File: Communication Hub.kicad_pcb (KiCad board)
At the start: 4 copper layers, 105 x 78.9 mm, 89 parts, among them J1 USB_B, J10 RS485, J11 RS422, J2 USB_A, J3 U5 TX RX, J4 U6 TX RX, J5 U7 TX RX, J6 RJ45, J7 RJ45, J8 RJ45, J9 CAN, U1 AMS1117-3.3, U10 MAX490E, U11 TPS2553DBVR, U12 TPS2553DBVR, U13 TPS2553DBVR, U2 USBLC6-2SC6, U3 USB2514B_Bi, U4 USBLC6-2SC6, U5 CP2102N-Axx-xQFN28, U6 CP2102N-Axx-xQFN28, U7 CP2102N-Axx-xQFN28, U8 TPS2553DBVR, U9 MAX3485, Y2 24Mhz

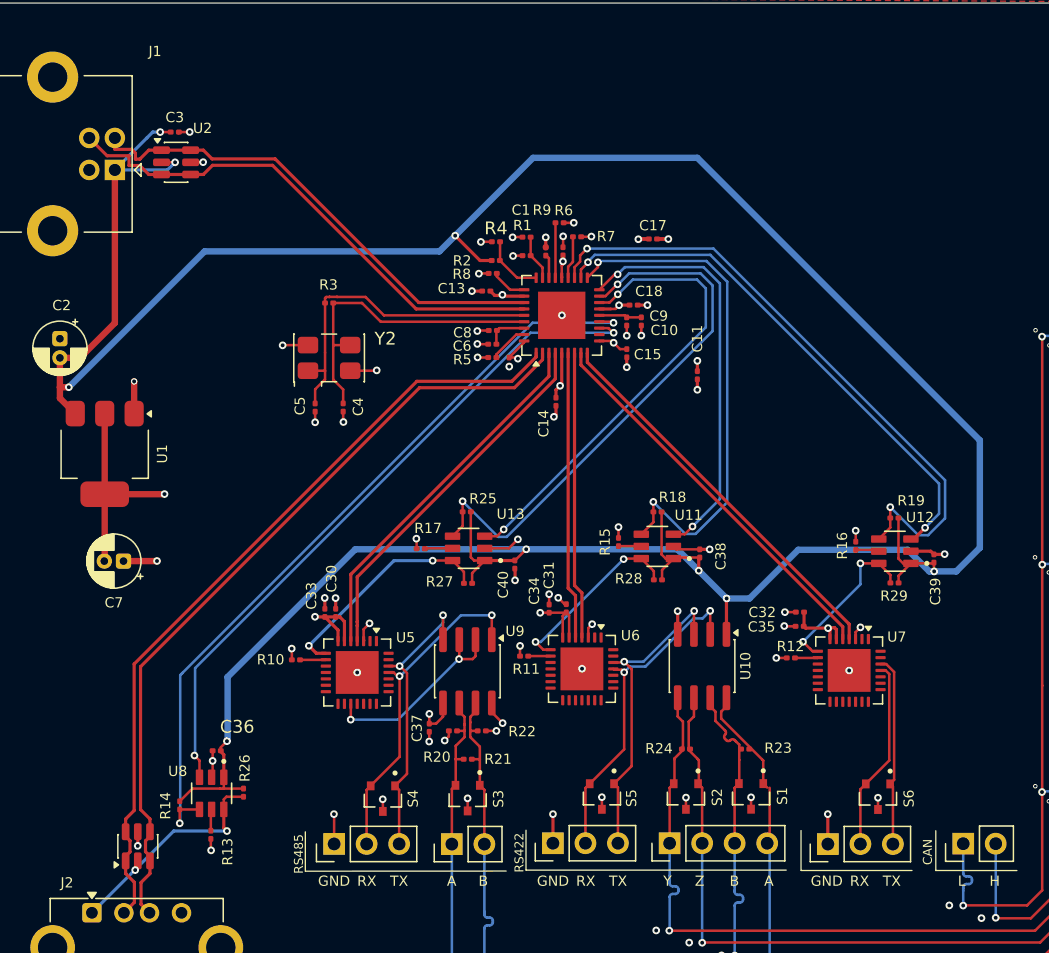
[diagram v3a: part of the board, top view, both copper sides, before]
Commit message: Corrections to PCB (modified passive components size) Corrections to schematics(addes some capacitors and other corrections)
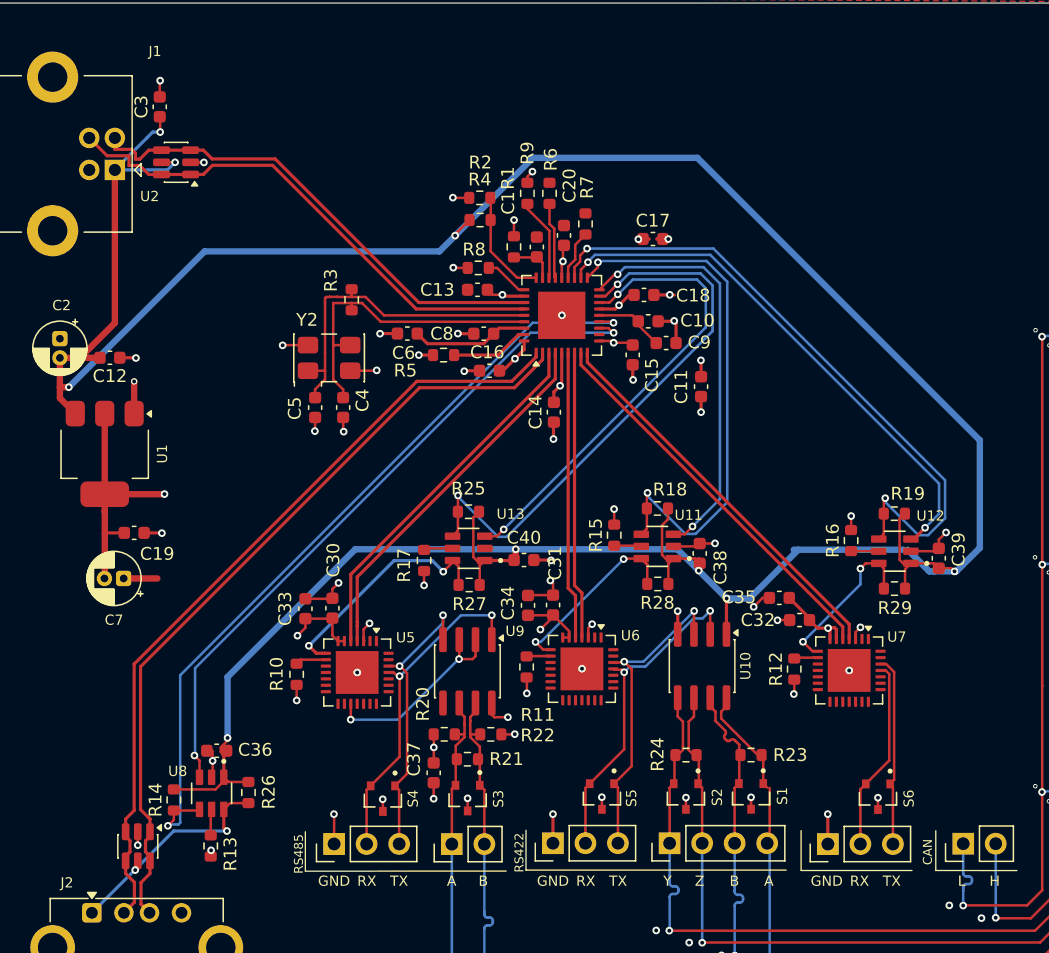
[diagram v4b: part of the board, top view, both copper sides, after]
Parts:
- added C12: 0.1uF, Capacitor_SMD:C_0603_1608Metric, F.Cu at (42.4, 88.0)
- added C19: 0.1uF, Capacitor_SMD:C_0603_1608Metric, F.Cu at (44.3, 101.6)
- C1, C10, C11, C13, C14, C15, C16, C17, C18, C20, C3, C30, C31, C32, C33, C34, C35, C36, C37, C38, C39, C4, C40, C5, C6, C8, C9: footprint Capacitor_SMD:C_0201_0603Metric -> Capacitor_SMD:C_0603_1608Metric
- R1, R10, R11, R12, R13, R14, R15, R16, R17, R18, R19, R2, R20, R21, R22, R23, R24, R25, R26, R27, R28, R29, R3, R4, R5, R6, R7, R8, R9: footprint Resistor_SMD:R_0201_0603Metric -> Resistor_SMD:R_0603_1608Metric
- moved C6 6.69 mm to (65.6, 86.1)
- moved R9 4.76 mm to (75.0, 75.1)
- moved R5 3.81 mm to (68.4, 87.7)
- moved R4 3.66 mm to (71.3, 75.5)
- moved C37 3.54 mm to (67.7, 120.4), turned to 90 degrees
- moved R2 3.39 mm to (71.3, 77.2)
- moved C35 2.73 mm to (94.7, 106.7)
- moved C9 2.57 mm to (85.8, 86.8), turned to 180 degrees
- moved R6 2.43 mm to (76.7, 75.1), turned to -90 degrees
- moved C3 2.30 mm to (46.3, 68.3), turned to 90 degrees
- moved R3 1.78 mm to (61.3, 83.4), turned to 90 degrees
- moved C16 1.68 mm to (72.0, 89.0), turned to 0 degrees
- moved C10 1.68 mm to (84.4, 85.1), turned to 180 degrees
- moved C34 1.67 mm to (75.0, 107.3)
- moved C33 1.55 mm to (57.6, 107.6)
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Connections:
- U2 pad 1: /DN -> /DP
- U2 pad 2: VBUS -> GND
- U2 pad 3: /DP -> /DN
- U2 pad 4: /DP -> /DN
- U2 pad 5: GND -> VBUS
- U2 pad 6: /DN -> /DP
- U4 pad 1: /USBA_DN -> /USBA_DP
- U4 pad 2: Net-(J2-VBUS) -> GND
- U4 pad 3: /USBA_DP -> /USBA_DN
- U4 pad 4: /USBA_DP -> /USBA_DN
- U4 pad 5: GND -> Net-(J2-VBUS)
- U4 pad 6: /USBA_DN -> /USBA_DP
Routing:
- net +3.3V: track 59.2 -> 69.4 mm, vias 20 -> 19
- net GND: track 73.2 -> 81.6 mm, vias 93 -> 85
- net Net-(U3-PLLFILT): track 3.29 -> 9.18 mm
- net Net-(U3-HS_IND/CFG_SEL1): track 1.88 -> 6.56 mm
- net Net-(U3-VBUS_DET): track 4.84 -> 8.60 mm
- net Net-(U3-RBIAS): track 3.05 -> 6.13 mm
- net VBUS: track 248.3 -> 250.6 mm
- net Net-(U3-CRFILT): track 3.38 -> 5.52 mm
- net Net-(U3-SCL/SMBCLK/CFG_SEL0): track 4.31 -> 5.97 mm
- net /OCS_N1: track 60.9 -> 62.4 mm
- net /OCS_N4: track 49.7 -> 51.1 mm
- net /OCS_N3: track 40.3 -> 41.4 mm
- net /OCS_N2: track 44.0 -> 45.0 mm
- net /VBUS2: track 17.7 -> 18.5 mm
- net /VBUS3: track 14.4 -> 15.2 mm
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
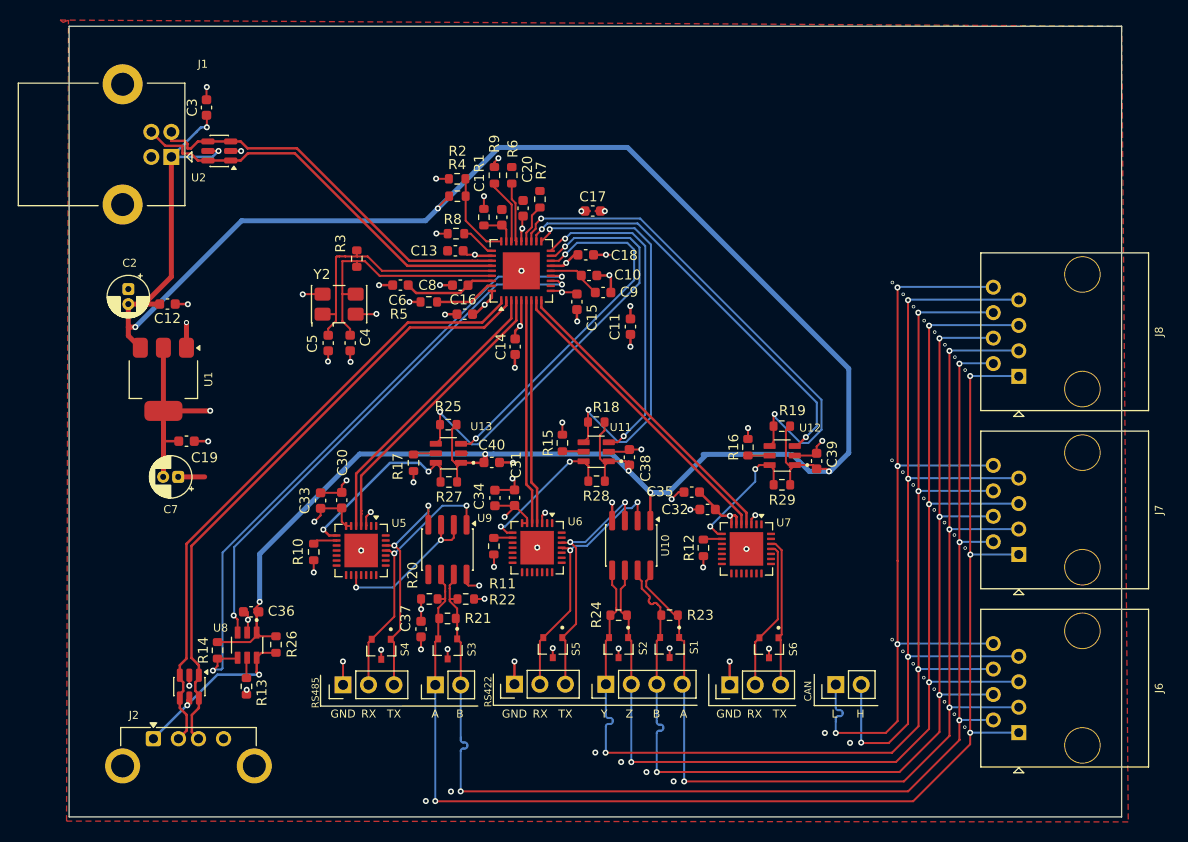
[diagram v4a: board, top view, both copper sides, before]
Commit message: Corrections to PCB (size optimization)
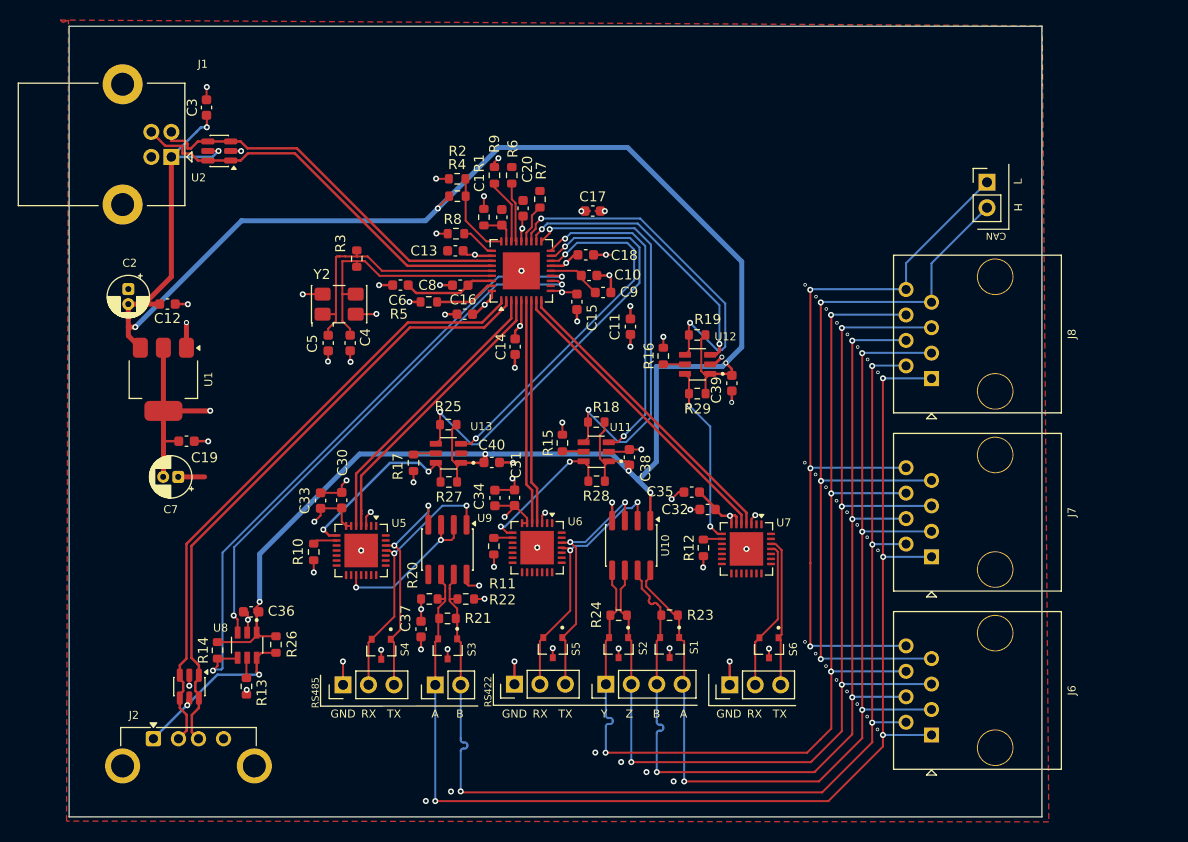
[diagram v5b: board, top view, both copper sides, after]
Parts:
- moved J9 52.3 mm to (124.1, 75.8), turned to 0 degrees
- moved U12 12.4 mm to (95.3, 94.0)
- moved R19 12.4 mm to (95.2, 91.0)
- moved R16 12.4 mm to (91.8, 93.1)
- moved R29 12.4 mm to (95.2, 96.9)
- moved C39 11.5 mm to (98.7, 95.8), turned to 90 degrees
- moved J6 8.70 mm to (118.6, 130.9)
- moved J7 8.70 mm to (118.6, 113.2)
- moved J8 8.70 mm to (118.6, 95.4)
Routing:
- net VBUS: track 250.6 -> 234.2 mm
- net /OCS_N4: track 51.1 -> 37.0 mm
- net /PRTPWR4: track 41.9 -> 28.7 mm
- net RS422 AB_P: track 110.2 -> 101.4 mm
- net RS485+: track 131.7 -> 122.9 mm
- net RS422 ZY_P: track 115.8 -> 107.1 mm
- net RS422 AB_N: track 107.9 -> 99.2 mm
- net RS422 ZY_N: track 117.9 -> 109.2 mm
- net RS485-: track 124.3 -> 115.6 mm
- net CAN H: track 86.7 -> 80.5 mm, vias 4 -> 3
- net CAN L: track 84.3 -> 78.2 mm, vias 4 -> 3
- net /VBUS4: track 12.8 -> 17.7 mm
- net GND: track 81.6 -> 80.5 mm, vias 85 -> 84
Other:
- board size 105 x 78.9 mm -> 97 x 78.9 mm

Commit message: Schematics reorganized
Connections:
- net /OCS_N1 renamed OCS_N1
- net /OCS_N2 renamed OCS_N2
- net /OCS_N3 renamed OCS_N3
- net /OCS_N4 renamed OCS_N4
- net /PRTPWR1 renamed PRTPWR1
- net /PRTPWR2 renamed PRTPWR2
- net /PRTPWR3 renamed PRTPWR3
- net /PRTPWR4 renamed PRTPWR4
- net /USBA_DN renamed USBA_DN
- net /USBA_DP renamed USBA_DP
- net /USD2_DN renamed USD2_DN
- net /USD2_DP renamed USD2_DP
- net /USD3_DN renamed USD3_DN
- net /USD3_DP renamed USD3_DP
- net /USD4_DN renamed USD4_DN
- net /USD4_DP renamed USD4_DP
- net /VBUS2 renamed VBUS2
- net /VBUS3 renamed VBUS3
- net /VBUS4 renamed VBUS4
